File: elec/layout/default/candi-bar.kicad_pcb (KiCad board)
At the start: 2 copper layers, 85 x 30 mm, 28 parts, among them J1 ?, J10 ?, J11 ?, J12 ?, J2 ?, J3 ?, J4 ?, J5 ?, J6 ?, J7 ?, J8 ?, J9 ?, U1 ?, U2 ?, U3 ?, U4 ?

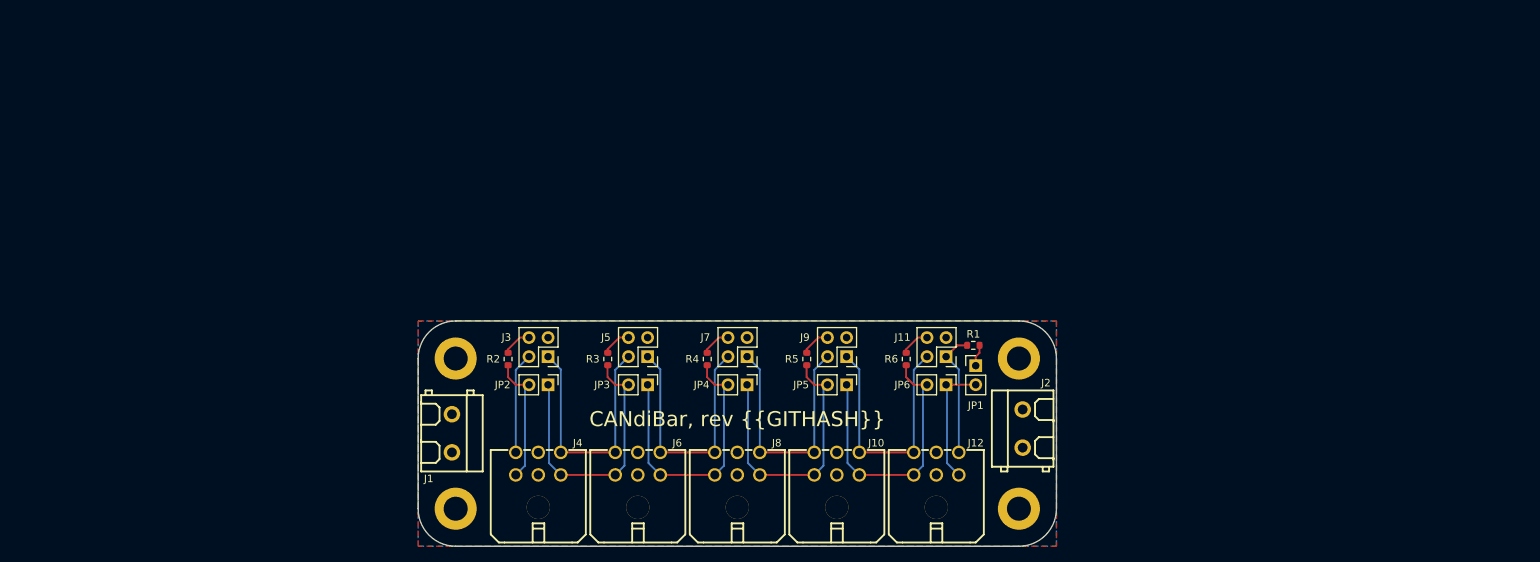
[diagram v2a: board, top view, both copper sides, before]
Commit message: feat: Add additional u2c circutry
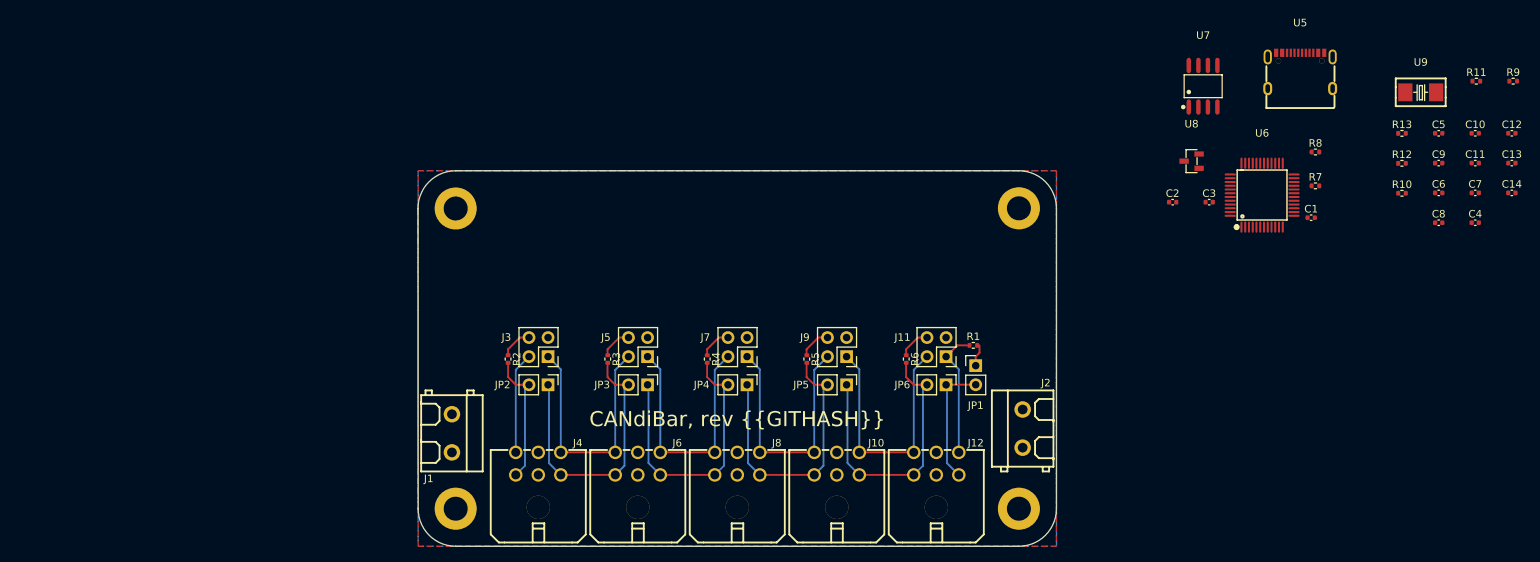
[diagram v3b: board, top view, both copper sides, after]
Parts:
- added C1: 10V 4.7uF X5R ±20% 0402 Multilayer Ceramic Capacitors MLCC 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, lib:C0402, F.Cu at (213.9, 56.2)
- added C10: 50V 4.7nF X7R ±10% 0402 Multilayer Ceramic Capacitors MLCC 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, lib:C0402, F.Cu at (235.8, 45.0)
- added C11: 16V 100nF X7R ±10% 0402 Multilayer Ceramic Capacitors MLCC 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, lib:C0402, F.Cu at (235.8, 49.0)
- added C12: 50V 22pF C0G ±5% 0402 Multilayer Ceramic Capacitors MLCC - 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, lib:C0402, F.Cu at (240.6, 45.0)
- added C13: 50V 22pF C0G ±5% 0402 Multilayer Ceramic Capacitors MLCC - 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, lib:C0402, F.Cu at (240.6, 49.0)
- added C14: 16V 100nF X7R ±10% 0402 Multilayer Ceramic Capacitors MLCC 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, lib:C0402, F.Cu at (240.6, 53.0)
- added C2: 10V 4.7uF X5R ±20% 0402 Multilayer Ceramic Capacitors MLCC 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, lib:C0402, F.Cu at (195.5, 54.2)
- added C3: 10V 4.7uF X5R ±20% 0402 Multilayer Ceramic Capacitors MLCC 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, lib:C0402, F.Cu at (200.3, 54.2)
- added C4: 16V 100nF X7R ±10% 0402 Multilayer Ceramic Capacitors MLCC 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, lib:C0402, F.Cu at (235.8, 56.9)
- added C5: 16V 100nF X7R ±10% 0402 Multilayer Ceramic Capacitors MLCC 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, lib:C0402, F.Cu at (230.9, 45.0)
- added C6: 16V 100nF X7R ±10% 0402 Multilayer Ceramic Capacitors MLCC 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, lib:C0402, F.Cu at (230.9, 53.0)
- added C7: 16V 100nF X7R ±10% 0402 Multilayer Ceramic Capacitors MLCC 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, lib:C0402, F.Cu at (235.8, 53.0)
- added C8: 16V 100nF X7R ±10% 0402 Multilayer Ceramic Capacitors MLCC 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, lib:C0402, F.Cu at (230.9, 56.9)
- added C9: 16V 100nF X7R ±10% 0402 Multilayer Ceramic Capacitors MLCC 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, lib:C0402, F.Cu at (230.9, 49.0)
- added R10: 62.5mW Thick Film Resistors 50V ±100ppm/℃ ±1% 60.4Ω 0402 Ch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, lib:R0402, F.Cu at (226.0, 53.0)
- added R11: 62.5mW Thick Film Resistors 50V ±1% ±100ppm/℃ 22Ω 0402 Chip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, lib:R0402, F.Cu at (235.9, 38.1)
- added R12: 62.5mW Thick Film Resistors 50V ±1% ±100ppm/℃ 22Ω 0402 Chip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, lib:R0402, F.Cu at (226.0, 49.0)
- added R13: 62.5mW Thick Film Resistors 50V ±100ppm/℃ ±1% 10kΩ 0402 Chi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, lib:R0402, F.Cu at (226.0, 45.0)
- added R7: 62.5mW Thick Film Resistors 50V ±100ppm/℃ ±1% 120Ω 0402 Chi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, lib:R0402, F.Cu at (214.5, 52.0)
- added R8: 62.5mW Thick Film Resistors 50V ±100ppm/℃ ±1% 10kΩ 0402 Chi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, lib:R0402, F.Cu at (214.5, 47.5)
- added R9: 62.5mW Thick Film Resistors 50V ±100ppm/℃ ±1% 60.4Ω 0402 Ch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, lib:R0402, F.Cu at (240.8, 38.1)
- added U5: ?, lib:USB-C-SMD_TYPE-C-6PIN-2MD-073, F.Cu at (212.5, 36.7)
- added U6: ?, lib:LQFP-48_L7.0-W7.0-P0.50-LS9.0-BL, F.Cu at (207.4, 53.2)
- added U7: ?, lib:SOIC-8_L4.9-W3.9-P1.27-LS6.0-BL, F.Cu at (199.5, 38.7)
- added U8: ?, lib:SOT-23-3_L2.9-W1.3-P1.90-LS2.4-BR, F.Cu at (198.0, 48.7)
- added U9: ?, lib:CRYSTAL-SMD_L5.0-W3.2, F.Cu at (228.5, 39.5)
- R1, R2: value 100mW Thick Film Resistors 75V ±100ppm/℃ ±1% 120Ω 0603 Chip Resistor - Surface Mount ROHS -> 62.5mW Thick Film Resistors 50V ±100ppm/℃ ±1% 5.1kΩ 0402 Chip Resistor - Surface Mount ROHS; footprint lib:R0603 -> lib:R0402
- R3, R4, R5, R6: value 100mW Thick Film Resistors 75V ±100ppm/℃ ±1% 120Ω 0603 Chip Resistor - Surface Mount ROHS -> 62.5mW Thick Film Resistors 50V ±100ppm/℃ ±1% 120Ω 0402 Chip Resistor - Surface Mount ROHS; footprint lib:R0603 -> lib:R0402
- moved U3 20.0 mm to (175.0, 55.0)
- moved U4 20.0 mm to (100.0, 55.0)
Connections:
- JP1 pad 1: p1 -> canl-1
- JP1 pad 2: canl-5 -> canl
- JP2 pad 1: canl-1 -> canl-2
- JP2 pad 2: canl -> canl-1
- JP3 pad 1: canl-2 -> canl-3
- JP3 pad 2: canl-1 -> canl-2
- JP4 pad 1: canl-3 -> canl-4
- JP4 pad 2: canl-2 -> canl-3
- JP5 pad 1: canl-4 -> canl-5
- JP5 pad 2: canl-3 -> canl-4
- R1 pad 1: canh-5 -> cc1
- R1 pad 2: p1 -> gnd
- R2 pad 1: port_1.r_term-p4 -> cc2
- R2 pad 2: canl -> gnd
- R3 pad 1: port_2.r_term-p4 -> port_1.r_term-p4
- R3 pad 2: canl-1 -> canl
- R4 pad 1: port_3.r_term-p4 -> port_2.r_term-p4
- R4 pad 2: canl-2 -> canl-1
- R5 pad 1: port_4.r_term-p4 -> port_3.r_term-p4
- R5 pad 2: canl-3 -> canl-2
- R6 pad 1: port_5.r_term-p4 -> port_4.r_term-p4
- R6 pad 2: canl-4 -> canl-3
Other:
- board size 85 x 30 mm -> 85 x 50 mm

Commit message: feat: Add u2c and pcb
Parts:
- removed the J10 at (150.8, 89.0)
- removed the J8 at (137.5, 89.0)
- removed JP2, JP3, JP4, JP5, JP6: ?, lib:PinHeader_1x02_P2.54mm_Vertical
- removed the R10 at (226.0, 53.0)
- removed the R13 at (226.0, 45.0)
- removed the R9 at (240.8, 38.1)
- added C1: 25V 1uF X5R ±10% 0402 Multilayer Ceramic Capacitors MLCC - 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, lib:C0402, F.Cu at (150.5, 61.5)
- added C2: 25V 1uF X5R ±10% 0402 Multilayer Ceramic Capacitors MLCC - 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, lib:C0402, F.Cu at (148.5, 62.5)
- added J1: ?, lib:PinHeader_2x02_P2.54mm_Vertical, F.Cu at (109.9, 73.0)
- added J13: ?, lib:PinHeader_2x02_P2.54mm_Vertical, F.Cu at (165.1, 70.5)
- added J14: ?, lib:CONN-TH_43045-0600, F.Cu at (170.4, 71.8)
- added J3: ?, lib:PinHeader_2x02_P2.54mm_Vertical, F.Cu at (112.3, 83.0)
- added J5: ?, lib:PinHeader_2x02_P2.54mm_Vertical, F.Cu at (125.5, 83.0)
- added J7: ?, lib:PinHeader_2x02_P2.54mm_Vertical, F.Cu at (138.8, 83.0)
- added R14: 62.5mW Thick Film Resistors 50V ±100ppm/℃ ±1% 120Ω 0402 Chi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, lib:R0402, F.Cu at (169.6, 63.5)
- added R3: 62.5mW Thick Film Resistors 50V ±100ppm/℃ ±1% 1kΩ 0402 Chip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, lib:R0402, F.Cu at (158.0, 73.2)
- added R4: 62.5mW Thick Film Resistors 50V ±100ppm/℃ ±1% 6.8kΩ 0402 Ch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, lib:R0402, F.Cu at (160.0, 73.2)
- added R5: 62.5mW Thick Film Resistors 50V ±100ppm/℃ ±1% 470Ω 0402 Chi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, lib:R0402, F.Cu at (156.0, 73.2)
- added U10: ?, lib:LED0603-RD, F.Cu at (158.0, 75.7)
- added U11: ?, lib:LED0603-RD, F.Cu at (160.0, 75.7)
- added U12: ?, lib:LED0603-RD, F.Cu at (156.0, 75.7)
- added U13: ?, lib:WSON-6_L2.0-W2.0-P0.65-TL-EP, F.Cu at (150.5, 63.9)
- added U15: ?, lib:HDR-TH_6P-P2.54-V-M-A, F.Cu at (137.5, 58.5)
- added U19: ?, lib:LED0603-RD, F.Cu at (152.0, 75.7)
- added U20: ?, lib:LED0603-RD, F.Cu at (154.0, 75.7)
- added U8: ?, lib:SOT-23-5_L2.9-W1.6-P0.95-LS2.8-BR, F.Cu at (150.0, 59.1)
- added U9: ?, lib:HDR-TH_4P-P2.54-V-M-1, F.Cu at (157.6, 66.1)
- J10: renamed from J7; footprint lib:PinHeader_2x02_P2.54mm_Vertical -> lib:CONN-TH_43045-0600
- J2: renamed from J3; footprint lib:PinHeader_2x02_P2.54mm_Vertical -> lib:CONN-TH_43045-0600
- J6: renamed from J5; footprint lib:PinHeader_2x02_P2.54mm_Vertical -> lib:CONN-TH_43045-0600
- R10: renamed from R7; value 62.5mW Thick Film Resistors 50V ±100ppm/℃ ±1% 120Ω 0402 Chip Resistor - Surface Mount ROHS -> 62.5mW Thick Film Resistors 50V ±1% ±100ppm/℃ 22Ω 0402 Chip Resistor - Surface Mount ROHS
- R11, R12: value 62.5mW Thick Film Resistors 50V ±1% ±100ppm/℃ 22Ω 0402 Chip Resistor - Surface Mount ROHS -> 62.5mW Thick Film Resistors 50V ±100ppm/℃ ±1% 470Ω 0402 Chip Resistor - Surface Mount ROHS
- R6: renamed from R3; value 62.5mW Thick Film Resistors 50V ±100ppm/℃ ±1% 120Ω 0402 Chip Resistor - Surface Mount ROHS -> 62.5mW Thick Film Resistors 50V ±100ppm/℃ ±1% 10kΩ 0402 Chip Resistor - Surface Mount ROHS
- R7: renamed from R4; value 62.5mW Thick Film Resistors 50V ±100ppm/℃ ±1% 120Ω 0402 Chip Resistor - Surface Mount ROHS -> 62.5mW Thick Film Resistors 50V ±100ppm/℃ ±1% 60.4Ω 0402 Chip Resistor - Surface Mount ROHS
- R8: renamed from R5; value 62.5mW Thick Film Resistors 50V ±100ppm/℃ ±1% 120Ω 0402 Chip Resistor - Surface Mount ROHS -> 62.5mW Thick Film Resistors 50V ±100ppm/℃ ±1% 60.4Ω 0402 Chip Resistor - Surface Mount ROHS
- R9: renamed from R6; value 62.5mW Thick Film Resistors 50V ±100ppm/℃ ±1% 120Ω 0402 Chip Resistor - Surface Mount ROHS -> 62.5mW Thick Film Resistors 50V ±1% ±100ppm/℃ 22Ω 0402 Chip Resistor - Surface Mount ROHS
- U5: renamed from J1; footprint lib:CONN-TH_2P-P5.08 -> lib:CONN-TH_2P-P5.00_DB129V-5.0-2P-BK-S
- U6: renamed from J2; footprint lib:CONN-TH_2P-P5.08 -> lib:CONN-TH_2P-P5.00_DB129V-5.0-2P-BK-S
- moved C12 122.5 mm to (115.0, 65.5), turned to 90 degrees
- moved C14 116.5 mm to (126.0, 66.0), turned to 90 degrees
- moved C15 116.2 mm to (126.0, 68.0), turned to -90 degrees
- moved U18 103.2 mm to (129.0, 67.0), turned to -90 degrees
- moved C6 103.1 mm to (133.0, 65.0), turned to -90 degrees
- moved C16 99.0 mm to (142.0, 61.0), turned to -90 degrees
- moved C10 98.6 mm to (133.0, 68.5), turned to 90 degrees
- moved C11 98.2 mm to (134.0, 65.0), turned to -90 degrees
- moved C13 92.8 mm to (146.0, 72.5), turned to -90 degrees
- moved R11 91.0 mm to (152.0, 73.2), turned to 90 degrees
- moved C9 90.9 mm to (145.5, 63.5)
- moved C7 90.2 mm to (145.0, 72.5), turned to -90 degrees
- moved U17 88.5 mm to (111.2, 66.0), turned to 90 degrees
- moved U16 86.3 mm to (116.0, 60.6), turned to 90 degrees
- moved C8 85.9 mm to (145.5, 62.5)
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- renumbered C8 to C10, C9 to C11, C10 to C12, C11 to C13, C12 to C14, C13 to C15, C14 to C16, C1 to C3, C2 to C4, C3 to C5, C4 to C6, C5 to C7, C6 to C8, C7 to C9, J6 to J8, R8 to R13, U6 to U14, U7 to U16, U8 to U17, U9 to U18, U5 to U7
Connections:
- C10 pad 1: candi_u2c-vcc -> vcc-1
- C11 pad 1: candi_u2c-vcc -> vcc-1
- C13 pad 1: candi_u2c-vcc -> vcc-1
- C3 pad 1: candi_u2c-vcc -> vcc-1
- C4 pad 1: candi_u2c-vcc -> vcc-1
- C5 pad 1: candi_u2c-vcc -> vcc-1
- C6 pad 1: candi_u2c-vcc -> vcc-1
- C7 pad 1: candi_u2c-vcc -> vcc-1
- C8 pad 1: candi_u2c-vcc -> vcc-1
- C9 pad 1: candi_u2c-vcc -> vcc-1
- J10 pad 1: canh-3 -> canh-5
- J10 pad 2: canh-2 -> vcc
- J10 pad 3: port_3.bypass_H-p3 -> canh-4
- J10 pad 4: port_3.r_term-p4 -> canl-5
- J11 pad 1: canh-5 -> canh-6
- J11 pad 2: canh-4 -> canh-5
- J11 pad 3: port_5.bypass_H-p3 -> canl-6
- J11 pad 4: port_5.r_term-p4 -> canl-5
- J12 pad 1: canl-5 -> canh-6
- J12 pad 2: gnd -> vcc
- J12 pad 3: canl-4 -> canh-5
- J12 pad 4: canh-5 -> canl-6
- J12 pad 5: vcc -> gnd
- J12 pad 6: canh-4 -> canl-5
- J2 pad 2: canh -> vcc
- J2 pad 3: port_1.bypass_H-p3 -> canh
- J2 pad 4: port_1.r_term-p4 -> canl-1
- J4 pad 1: canl-1 -> canh-2
- J4 pad 2: gnd -> vcc
- J4 pad 3: canl -> canh-1
- J4 pad 4: canh-1 -> canl-2
- J4 pad 5: vcc -> gnd
- J4 pad 6: canh -> canl-1
- J6 pad 1: canh-2 -> canh-3
- J6 pad 2: canh-1 -> vcc
- J6 pad 3: port_2.bypass_H-p3 -> canh-2
- J6 pad 4: port_2.r_term-p4 -> canl-3
- J8 pad 1: canl-2 -> canh-4
- J8 pad 2: gnd -> vcc
- J8 pad 3: canl-1 -> canh-3
- J8 pad 4: canh-2 -> canl-4
- J8 pad 5: vcc -> gnd
- J8 pad 6: canh-1 -> canl-3
- J9 pad 1: canh-4 -> canh-5
- J9 pad 2: canh-3 -> canh-4
- J9 pad 3: port_4.bypass_H-p3 -> canl-5
- J9 pad 4: port_4.r_term-p4 -> canl-4
- JP1 pad 1: canl-1 -> p1
- JP1 pad 2: canl -> canl-7
- R10 pad 1: port_5.r_term-p4 -> pa11
- R10 pad 2: canl-4 -> dm
- R11 pad 1: pa12 -> candi_u2c.status_1.LED-a
- R11 pad 2: dp -> pa0
- R12 pad 1: pa11 -> candi_u2c.status_2.LED-a
- R12 pad 2: dm -> pa1
- R13 pad 1: boot0 -> nrst
- R13 pad 2: gnd -> vcc-1
- R6 pad 1: port_1.r_term-p4 -> boot0
- R6 pad 2: canl -> gnd
- R7 pad 1: port_2.r_term-p4 -> canh
- R7 pad 2: canl-1 -> candi_u2c.can_trx.ic-vcc
- R8 pad 1: port_3.r_term-p4 -> canl
- R8 pad 2: canl-2 -> candi_u2c.can_trx.ic-vcc
- R9 pad 1: port_4.r_term-p4 -> pa12
- R9 pad 2: canl-3 -> dp
- U14 pad 1: candi_u2c-vcc -> vcc-1
- U14 pad 24: candi_u2c-vcc -> vcc-1
- U14 pad 36: candi_u2c-vcc -> vcc-1
- U14 pad 48: candi_u2c-vcc -> vcc-1
- U14 pad 9: candi_u2c-vcc -> vcc-1
- U16 pad 3: candi_u2c-vcc -> vcc-1
- U16 pad 6: canl-5 -> canl
- U16 pad 7: canh-5 -> canh
- U17 pad 1: canl-5 -> canl
- U17 pad 2: canh-5 -> canh
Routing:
- net vcc-1: track 0.00 -> 105.8 mm, vias 0 -> 5
- net gnd: track 0.00 -> 57.8 mm, vias 0 -> 43
- net pa1: track 0.00 -> 39.0 mm
- net usb_j1-vcc: track 0.00 -> 38.2 mm, vias 0 -> 4
- net pa0: track 0.00 -> 37.3 mm
- net canh-6: track 0.00 -> 32.3 mm
- net canl-6: track 0.00 -> 27.1 mm
- net pb8: track 0.00 -> 24.9 mm
- net pb9: track 0.00 -> 24.5 mm
- net dm: track 0.00 -> 24.0 mm, vias 0 -> 1
- net canh: track 13.5 -> 32.9 mm
- net dp: track 0.00 -> 17.4 mm
- net nrst: track 0.00 -> 16.2 mm, vias 0 -> 1
- net canl-2: track 37.5 -> 21.5 mm
- net canl-3: track 37.5 -> 21.5 mm
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- added copper zone on F.Cu, net gnd
- added copper zone on In1.Cu, net gnd
- added copper zone on In2.Cu, net gnd
- added copper zone on B.Cu, net vcc
- removed copper zone on B.Cu, net gnd
- removed copper zone on F.Cu, net vcc
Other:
- board size 85 x 50 mm -> 88 x 44 mm
- copper layers 2 -> 4

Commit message: feat: Semifinal design
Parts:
- added REF**: OSHW-Logo2_7.3x6mm_SilkScreen, Symbol:OSHW-Logo2_7.3x6mm_SilkScreen, F.Cu at (121.8, 72.5)
- added REF**: WEEE-Logo_4.2x6mm_SilkScreen, Symbol:WEEE-Logo_4.2x6mm_SilkScreen, B.Cu at (116.5, 75.5)
- moved R11 1.50 mm to (152.0, 71.7)
- moved R12 1.50 mm to (154.0, 71.7)
- moved R3 1.50 mm to (158.0, 71.7)
- moved R4 1.50 mm to (160.0, 71.7)
- moved R5 1.50 mm to (156.0, 71.7)
- moved U10 1.50 mm to (158.0, 74.2)
- moved U11 1.50 mm to (160.0, 74.2)
- moved U12 1.50 mm to (156.0, 74.2)
- moved U19 1.50 mm to (152.0, 74.2)
- moved U20 1.50 mm to (154.0, 74.2)
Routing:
- net canl-4: track 21.5 -> 7.25 mm
- net canl-5: track 21.5 -> 7.25 mm
- net canl-3: track 21.5 -> 7.25 mm
- net canl-1: track 27.2 -> 13.0 mm
- net canl-2: track 21.5 -> 7.25 mm
- net canl-6: track 27.1 -> 12.9 mm
- net vcc-1: track 105.8 -> 92.5 mm
- net canh-1: track 32.3 -> 22.1 mm
- net canh-3: track 22.4 -> 12.1 mm
- net canh-6: track 32.3 -> 22.1 mm
- net canh-5: track 22.4 -> 12.1 mm
- net canh-4: track 22.4 -> 12.1 mm
- net canh-2: track 22.4 -> 12.1 mm
- net gnd: track 57.8 -> 65.3 mm, vias 43 -> 75
- net canl: track 22.9 -> 15.7 mm
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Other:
- board text added: "- +"
- board text added: "CANdiBar"
- board text added: "CANdiBar, rev {{GITHASH}} https://github.com/CRTified/CANdiBar MIT License"
- board text added: "GND 3.3V BOOT0 NRST SWCLK SWDIO"
- board text added: "L-L H-H"
- board text added: "S1 S2 3.3 5.0 Vin"
- board text added: "TERM"
- board text removed: "CANdiBar, rev {{GITHASH}}"

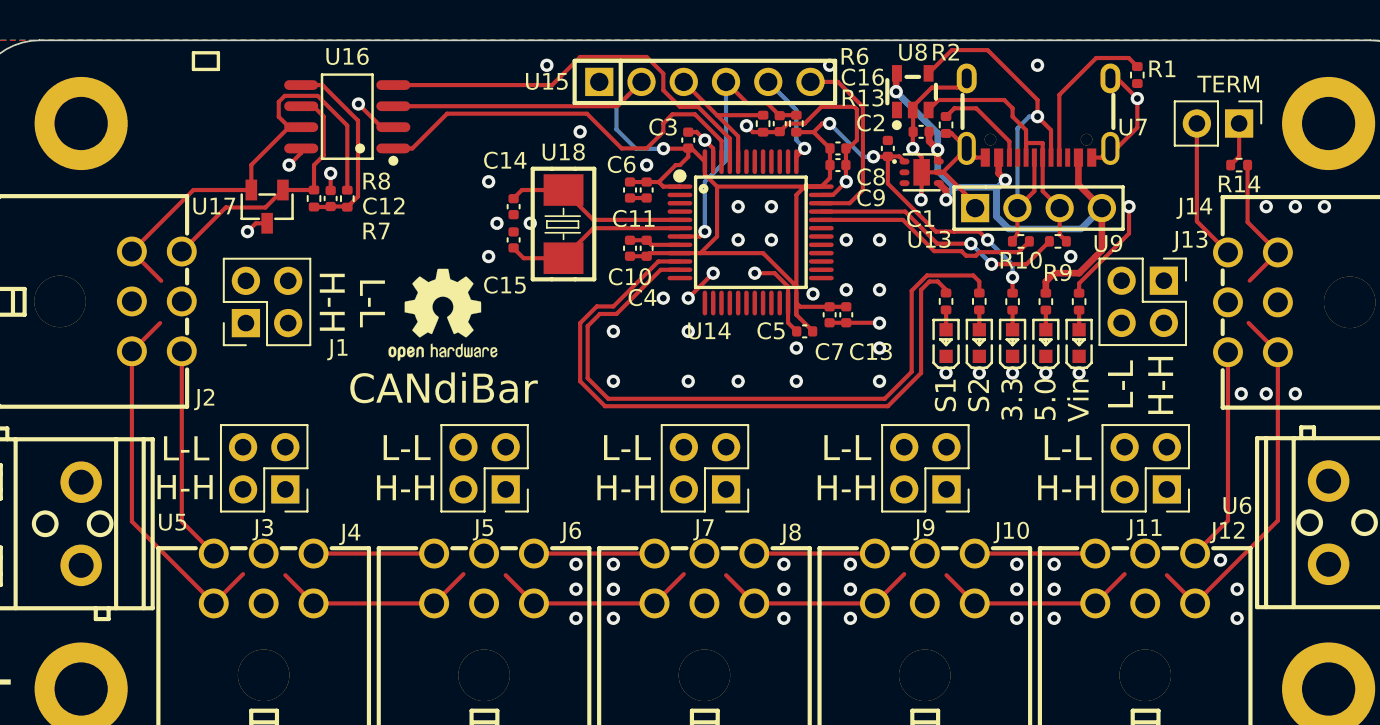
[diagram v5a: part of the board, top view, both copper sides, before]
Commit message: feat: Reworked with SMD Jumpering
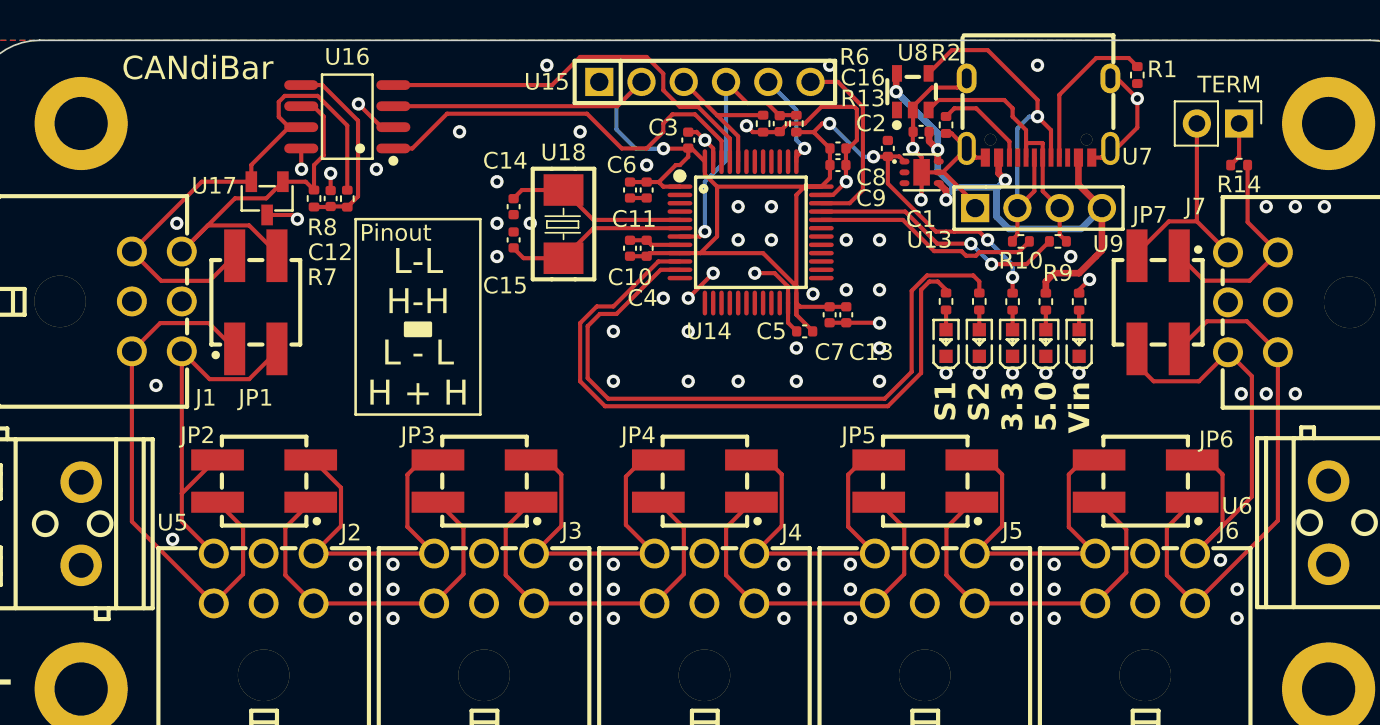
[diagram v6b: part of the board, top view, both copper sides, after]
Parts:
- removed REF**: OSHW-Logo2_7.3x6mm_SilkScreen, Symbol:OSHW-Logo2_7.3x6mm_SilkScreen
- removed REF**: WEEE-Logo_4.2x6mm_SilkScreen, Symbol:WEEE-Logo_4.2x6mm_SilkScreen
- JP1: renamed from J1; footprint lib:PinHeader_2x02_P2.54mm_Vertical -> lib:HDR-SMD_4P-P2.54-V-M-R2-C2-LS7.5
- JP2: renamed from J3; footprint lib:PinHeader_2x02_P2.54mm_Vertical -> lib:HDR-SMD_4P-P2.54-V-M-R2-C2-LS7.5
- JP3: renamed from J5; footprint lib:PinHeader_2x02_P2.54mm_Vertical -> lib:HDR-SMD_4P-P2.54-V-M-R2-C2-LS7.5
- JP4: renamed from J7; footprint lib:PinHeader_2x02_P2.54mm_Vertical -> lib:HDR-SMD_4P-P2.54-V-M-R2-C2-LS7.5
- JP5: renamed from J9; footprint lib:PinHeader_2x02_P2.54mm_Vertical -> lib:HDR-SMD_4P-P2.54-V-M-R2-C2-LS7.5
- JP6: renamed from J11; footprint lib:PinHeader_2x02_P2.54mm_Vertical -> lib:HDR-SMD_4P-P2.54-V-M-R2-C2-LS7.5
- JP7: renamed from J13; footprint lib:PinHeader_2x02_P2.54mm_Vertical -> lib:HDR-SMD_4P-P2.54-V-M-R2-C2-LS7.5
- moved JP1 1.38 mm to (110.5, 71.8), turned to 0 degrees
- moved JP2 1.37 mm to (111.0, 82.5), turned to 90 degrees
- moved JP3 1.37 mm to (124.2, 82.5), turned to 90 degrees
- moved JP4 1.37 mm to (137.5, 82.5), turned to 90 degrees
- moved JP5 1.37 mm to (150.8, 82.5), turned to 90 degrees
- moved JP6 1.37 mm to (164.0, 82.5), turned to 90 degrees
- moved JP7 1.34 mm to (164.8, 71.8), turned to 180 degrees
- moved U17 0.50 mm to (111.2, 65.5)
- renumbered J2 to J1, J4 to J2, J6 to J3, J8 to J4, J10 to J5, J12 to J6, J14 to J7, JP1 to JP8
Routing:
- net canl-6: track 12.9 -> 29.3 mm
- net canl-3: track 7.25 -> 22.6 mm
- net canl-4: track 7.25 -> 22.5 mm
- net canl-5: track 7.25 -> 22.5 mm
- net canl-2: track 7.25 -> 22.0 mm
- net canl-1: track 13.0 -> 23.2 mm
- net canh-1: track 22.1 -> 32.2 mm
- net canh-5: track 12.1 -> 22.2 mm
- net canh-4: track 12.1 -> 22.1 mm
- net canh-3: track 12.1 -> 22.1 mm
- net canh-2: track 12.1 -> 22.1 mm
- net canh-6: track 22.1 -> 32.0 mm
- net canl: track 15.7 -> 23.4 mm
- net vcc: track 6.44 -> 1.08 mm
- net canh-7: track 8.41 -> 13.3 mm
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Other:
- board text added: "L - L H + H"
- board text added: "Pinout"

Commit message: fix: Make silkscreen less ambigous
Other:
- board text added: "L L H H"
- board text removed: "L-L H-H"
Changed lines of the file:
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@@
 		)
 	)
-	(gr_text "L-L\nH-H"
+	(gr_text "L L\nH H"
 		(at 120.25 70.5 0)
 		(layer "F.SilkS" knockout)
@@
 			)
 		)
-		(render_cache "L-L\nH-H" 0
+		(render_cache "L L\nH H" 0
 			(polygon
 				(pts
 					(xy 118.647339 69.8625) (xy 119.466255 69.8625) (xy 119.489428 69.700841) (xy 118.827865 69.700841)
 					(xy 118.827865 68.414628) (xy 118.647339 68.414628)
-				)
-			)
-			(polygon
-				(pts
-					(xy 119.882995 69.280988) (xy 120.618013 69.280988) (xy 120.618013 69.129771) (xy 119.882995 69.129771)
 				)
 			)
@@
 				)
 			)
-			(polygon
-				(pts
-					(xy 119.882995 71.800988) (xy 120.618013 71.800988) (xy 120.618013 71.649771) (xy 119.882995 71.649771)
-				)
-			)
